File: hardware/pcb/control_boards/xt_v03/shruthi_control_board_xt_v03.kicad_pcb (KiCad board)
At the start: 2 copper layers, 286 x 99.4 mm, 125 parts, among them IC1 24LC512, IC10 ATMEGA644p, IC2 74HC165, IC3 74HC165, IC4 4051, IC5 4051, IC6 4051, IC7 4051, IC8 74HC595, IC9 74HC165, J1 Conn_01x08, J2 Conn_01x06, Q1 20MHz, SW1 Encoder, U1 AVR ISP, X1 MIDI, X2 MIDI

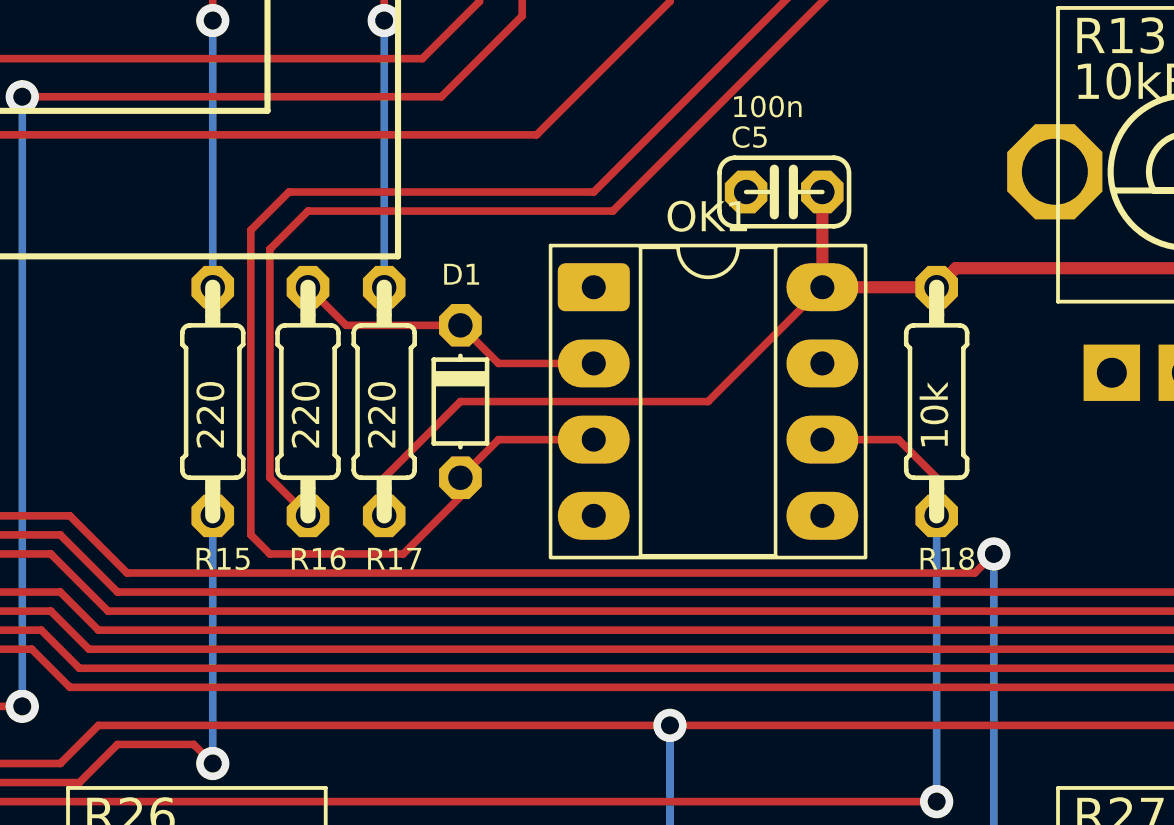
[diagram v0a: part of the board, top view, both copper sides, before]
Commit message: update footprints and silkscreen for optocoupler circuitry
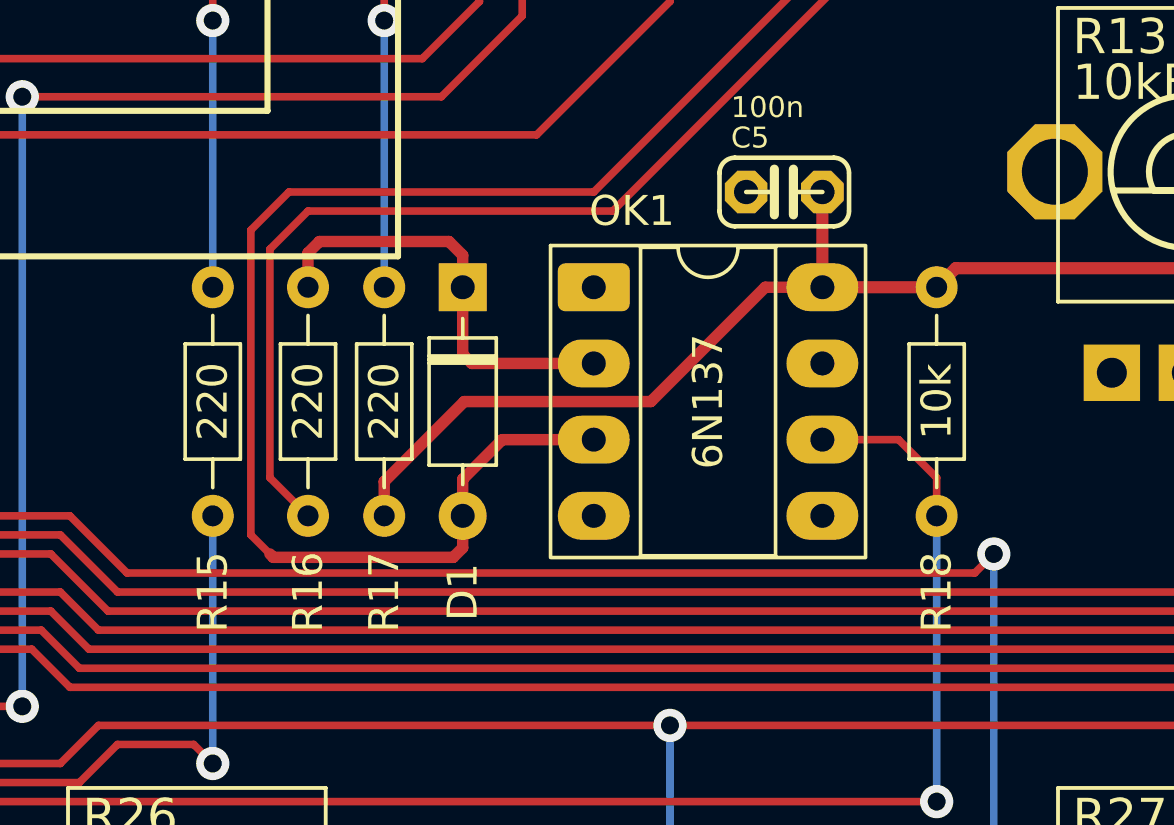
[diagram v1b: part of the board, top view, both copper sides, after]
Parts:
- D1: footprint shruthi_control_board_xt_v03:D-5 -> Diode_THT:D_DO-35_SOD27_P7.62mm_Horizontal
- R15, R16, R17, R18: footprint shruthi_control_board_xt_v03:0204_7 -> Resistor_THT:R_Axial_DIN0204_L3.6mm_D1.6mm_P7.62mm_Horizontal
- moved D1 3.81 mm to (255.7, 135.9)
- moved R15 3.81 mm to (247.4, 135.9)
- moved R16 3.81 mm to (250.6, 143.5)
- moved R17 3.81 mm to (253.1, 135.9)
- moved R18 3.81 mm to (271.5, 135.9)
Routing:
- net Net-(D1-K): track 10.6 -> 14.4 mm
- net Net-(D1-A): track 79.7 -> 80.8 mm

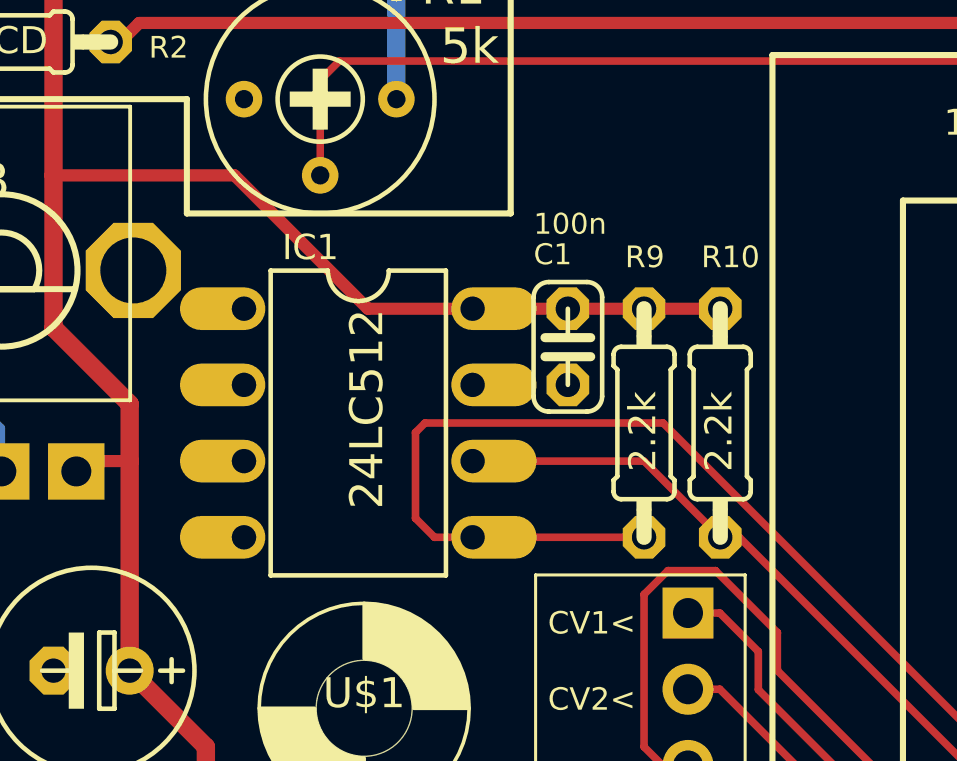
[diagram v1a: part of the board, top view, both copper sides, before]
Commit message: update footprints and silkscreen for 24LC512 circuitry
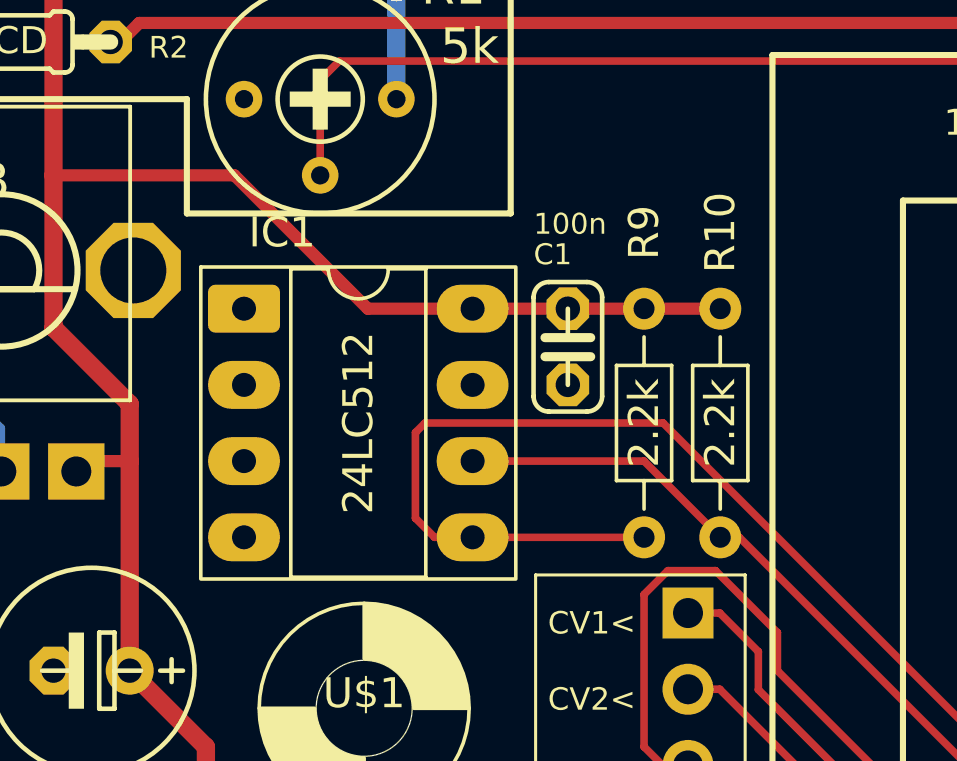
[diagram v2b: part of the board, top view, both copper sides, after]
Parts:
- IC1: footprint shruthi_control_board_xt_v03:DIL08 -> Package_DIP:DIP-8_W7.62mm_Socket_LongPads
- R10, R9: footprint shruthi_control_board_xt_v03:0204_7 -> Resistor_THT:R_Axial_DIN0204_L3.6mm_D1.6mm_P7.62mm_Horizontal
- moved IC1 5.39 mm to (156.0, 107.3), turned to 0 degrees
- moved R10 3.81 mm to (171.8, 114.9), turned to 90 degrees
- moved R9 3.81 mm to (169.3, 107.3)
